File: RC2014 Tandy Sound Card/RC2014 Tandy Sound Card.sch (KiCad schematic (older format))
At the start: 15 parts, among them J1 CONN_01X39, J2 Line Out, J3 Speaker Out, J4 CONN_02X08, U1 74LS138, U2 74LS245, U3 SN76489AN, U4 TDA7056A

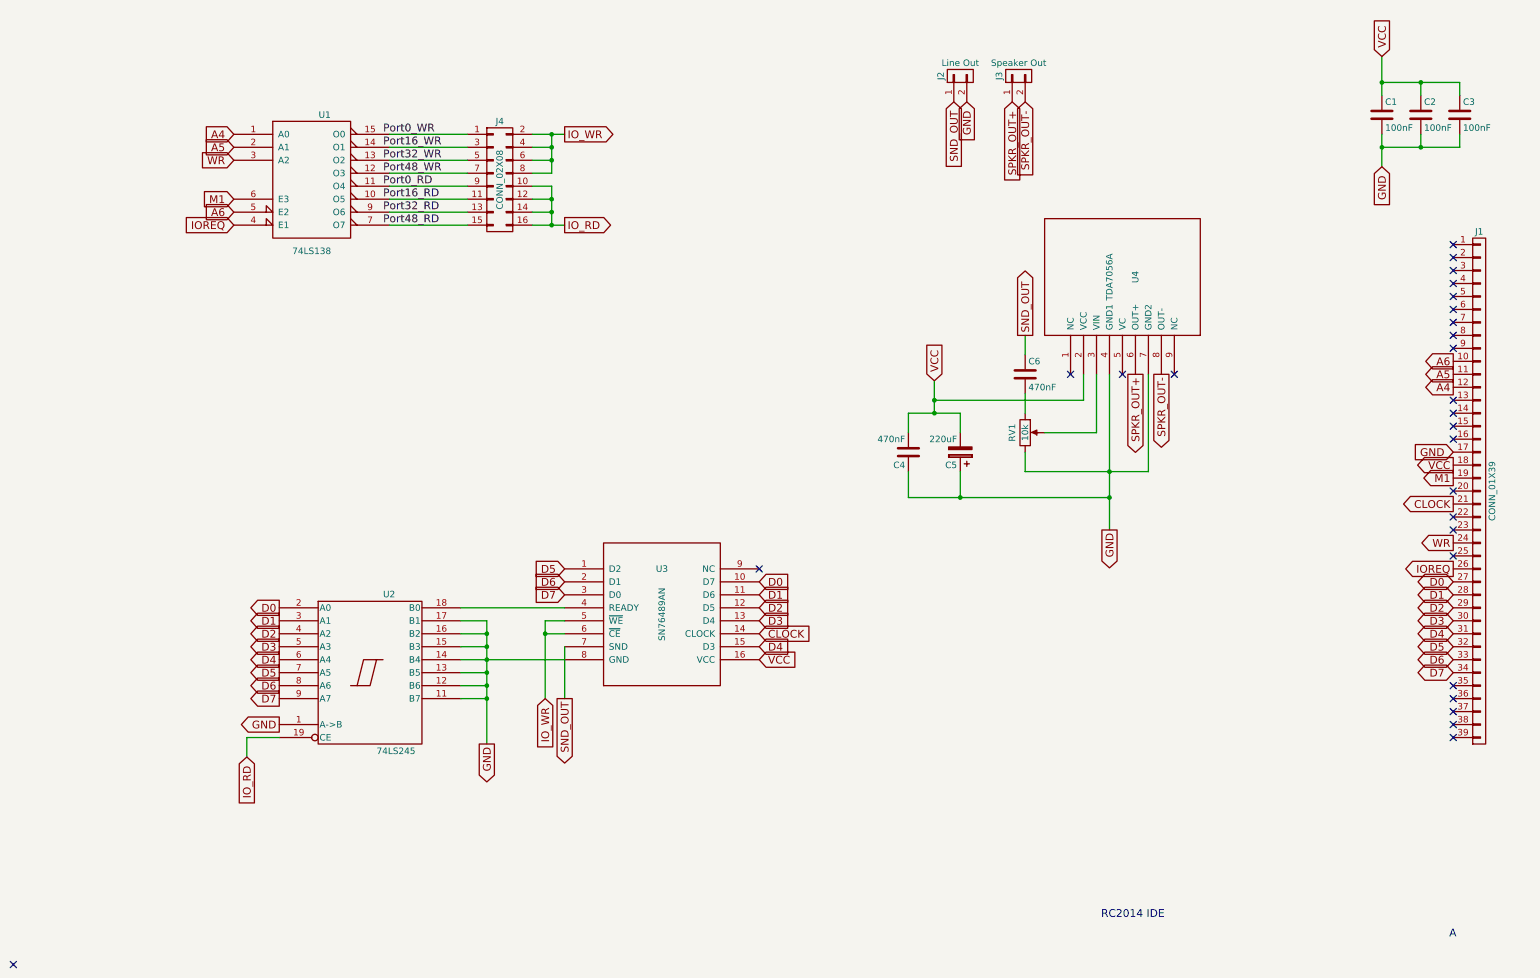
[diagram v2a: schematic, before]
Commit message: Added volume control
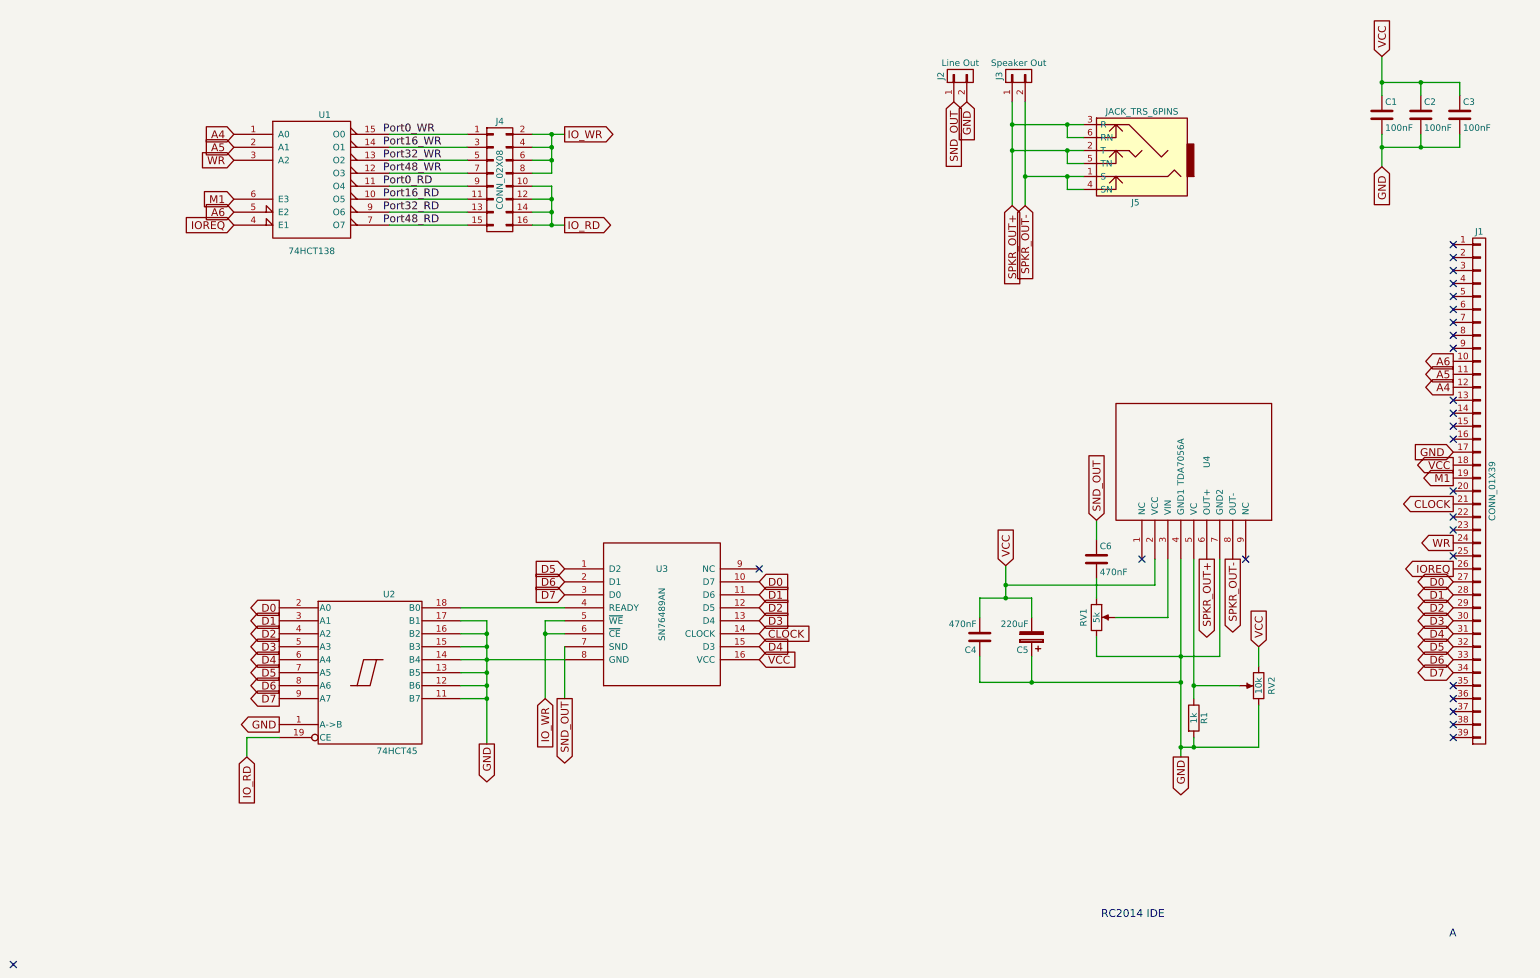
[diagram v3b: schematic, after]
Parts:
- added J5: JACK_TRS_6PINS, symbol JACK_TRS_6PINS
- added R1: 1k, symbol R
- added RV2: 10k, Potentiometers:Potentiometer_Trimmer_Bourns_3296W, symbol POT
- RV1: value 10k -> 5k
- U1: value 74LS138 -> 74HCT138
- U2: value 74LS245 -> 74HCT45
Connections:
- net GND: now also R1.2, RV2.1
- net SPKR_OUT+: now also J5.2 (T), J5.3 (R), J5.5 (TN), J5.6 (RN)
- net SPKR_OUT-: now also J5.1 (S), J5.4 (SN)
- net VCC: now also RV2.3
- net at U4.5 (VC): now also R1.1, RV2.2
- no-connect marks 27 -> 26
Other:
- moved on the sheet: C4, C5, C6, RV1, U4
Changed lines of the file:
@@
 P 1800 1800
 F 0 "U1" H 1900 2300 50  0000 C CNN
-F 1 "74LS138" H 1800 1250 50  0000 C CNN
+F 1 "74HCT138" H 1800 1250 50  0000 C CNN
 F 2 "Housings_DIP:DIP-16_W7.62mm_Socket" H 1800 1800 50  0001 C CNN
 F 3 "" H 1800 1800 50  0001 C CNN
@@
 P 2250 5600
 F 0 "U2" H 2350 6175 50  0000 L BNN
-F 1 "74LS245" H 2300 5025 50  0000 L TNN
+F 1 "74HCT45" H 2300 5025 50  0000 L TNN
 F 2 "Housings_DIP:DIP-20_W7.62mm_Socket" H 2250 5600 50  0001 C CNN
 F 3 "" H 2250 5600 50  0001 C CNN
@@
 L TDA7056A U4
 U 1 1 5917EAD4
-P 8050 2550
-F 0 "U4" H 8050 2450 50  0000 C CNN
-F 1 "TDA7056A" H 8050 2650 50  0000 C CNN
-F 2 "Pin_Headers:Pin_Header_Straight_1x09_Pitch2.54mm" H 8050 2550 50  0001 C CNN
-F 3 "DOCUMENTATION" H 8050 2550 50  0001 C CNN
-	1    8050 2550
+P 8600 3975
+F 0 "U4" H 8600 3875 50  0000 C CNN
+F 1 "TDA7056A" H 8600 4075 50  0000 C CNN
+F 2 "Pin_Headers:Pin_Header_Straight_1x09_Pitch2.54mm" H 8600 3975 50  0001 C CNN
+F 3 "DOCUMENTATION" H 8600 3975 50  0001 C CNN
+	1    8600 3975
 	0    -1   -1   0
 $EndComp
@@
 	0    -1   -1   0
 $EndComp
-Text GLabel 7950 4500 3    60   Output ~ 0
+Text GLabel 8500 6250 3    60   Output ~ 0
 GND
-Text GLabel 7200 1200 3    60   Input ~ 0
+Text GLabel 7200 2000 3    60   Input ~ 0
 SPKR_OUT+
-Text GLabel 7300 1200 3    60   Input ~ 0
+Text GLabel 7300 2000 3    60   Input ~ 0
 SPKR_OUT-
-Text GLabel 8150 3300 3    60   Output ~ 0
+Text GLabel 8700 4725 3    60   Output ~ 0
 SPKR_OUT+
-Text GLabel 8350 3300 3    60   Output ~ 0
+Text GLabel 8900 4725 3    60   Output ~ 0
 SPKR_OUT-
-Text GLabel 6600 3350 1    60   Input ~ 0
+Text GLabel 7150 4775 1    60   Input ~ 0
 VCC
-NoConn ~ 7650 3300
-NoConn ~ 8450 3300
+NoConn ~ 8200 4725
+NoConn ~ 9000 4725
 $Comp
 L C C6
 U 1 1 591812F7
-P 7300 3300
-F 0 "C6" H 7325 3400 50  0000 L CNN
-F 1 "470nF" H 7325 3200 50  0000 L CNN
-F 2 "Capacitors_THT:C_Disc_D4.7mm_W2.5mm_P5.00mm" H 7338 3150 50  0001 C CNN
-F 3 "" H 7300 3300 50  0001 C CNN
-	1    7300 3300
+P 7850 4725
+F 0 "C6" H 7875 4825 50  0000 L CNN
+F 1 "470nF" H 7875 4625 50  0000 L CNN
+F 2 "Capacitors_THT:C_Disc_D4.7mm_W2.5mm_P5.00mm" H 7888 4575 50  0001 C CNN
+F 3 "" H 7850 4725 50  0001 C CNN
+	1    7850 4725
 	1    0    0    -1
 $EndComp
@@
 L POT RV1
 U 1 1 591821C0
-P 7300 3750
-F 0 "RV1" V 7200 3750 50  0000 C CNN
-F 1 "10k" V 7300 3750 50  0000 C CNN
-F 2 "Potentiometers:Potentiometer_Trimmer_Bourns_3296W" H 7300 3750 50  0001 C CNN
-F 3 "" H 7300 3750 50  0001 C CNN
-	1    7300 3750
-	1    0    0    -1
-$EndComp
-Text GLabel 7300 3000 1    60   Output ~ 0
+P 7850 5175
+F 0 "RV1" V 7750 5175 50  0000 C CNN
+F 1 "5k" V 7850 5175 50  0000 C CNN
+F 2 "Potentiometers:Potentiometer_Trimmer_Bourns_3296W" H 7850 5175 50  0001 C CNN
+F 3 "" H 7850 5175 50  0001 C CNN
+	1    7850 5175
+	1    0    0    -1
+$EndComp
+Text GLabel 7850 4425 1    60   Input ~ 0
 SND_OUT
 $Comp
 L C C4
 U 1 1 59182F48
-P 6400 3900
-F 0 "C4" H 6425 4000 50  0000 L CNN
-F 1 "470nF" H 6425 3800 50  0000 L CNN
-F 2 "Capacitors_THT:C_Disc_D4.7mm_W2.5mm_P5.00mm" H 6438 3750 50  0001 C CNN
-F 3 "" H 6400 3900 50  0001 C CNN
-	1    6400 3900
+P 6950 5325
+F 0 "C4" H 6975 5425 50  0000 L CNN
+F 1 "470nF" H 6975 5225 50  0000 L CNN
+F 2 "Capacitors_THT:C_Disc_D4.7mm_W2.5mm_P5.00mm" H 6988 5175 50  0001 C CNN
+F 3 "" H 6950 5325 50  0001 C CNN
+	1    6950 5325
 	-1   0    0    1
 $EndComp
@@
 L CP C5
 U 1 1 59182FE8
-P 6800 3900
-F 0 "C5" H 6825 4000 50  0000 L CNN
-F 1 "220uF" H 6825 3800 50  0000 L CNN
-F 2 "Capacitors_THT:CP_Radial_D5.0mm_P2.00mm" H 6838 3750 50  0001 C CNN
-F 3 "" H 6800 3900 50  0001 C CNN
-	1    6800 3900
+P 7350 5325
+F 0 "C5" H 7375 5425 50  0000 L CNN
+F 1 "220uF" H 7375 5225 50  0000 L CNN
+F 2 "Capacitors_THT:CP_Radial_D5.0mm_P2.00mm" H 7388 5175 50  0001 C CNN
+F 3 "" H 7350 5325 50  0001 C CNN
+	1    7350 5325
 	-1   0    0    1
 $EndComp
-NoConn ~ 8050 3300
 $Comp
 L CONN_02X08 J4
@@
 Connection ~ 10350 1050
 Wire Wire Line
-	7950 3300 7950 4500
-Wire Wire Line
-	8250 4050 8250 3300
-Wire Wire Line
-	7300 4050 8250 4050
-Connection ~ 7950 4050
-Wire Wire Line
-	7450 3750 7850 3750
-Wire Wire Line
-	7850 3750 7850 3300
-Wire Wire Line
-	7300 3000 7300 3150
-Wire Wire Line
-	7300 3450 7300 3600
-Wire Wire Line
-	7300 3900 7300 4050
-Wire Wire Line
-	6600 3500 7750 3500
-Wire Wire Line
-	7750 3500 7750 3300
-Wire Wire Line
-	6400 3600 6800 3600
-Wire Wire Line
-	6800 3600 6800 3750
-Wire Wire Line
-	6400 4250 7950 4250
-Wire Wire Line
-	6800 4250 6800 4050
-Connection ~ 7950 4250
-Connection ~ 6800 4250
-Wire Wire Line
-	6400 3600 6400 3750
-Wire Wire Line
-	6400 4050 6400 4250
-Wire Wire Line
-	6600 3350 6600 3600
-Connection ~ 6600 3600
-Connection ~ 6600 3500
+	8500 4725 8500 6250
+Wire Wire Line
+	8800 5475 8800 4725
+Wire Wire Line
+	7850 5475 8800 5475
+Connection ~ 8500 5475
+Wire Wire Line
+	8000 5175 8400 5175
+Wire Wire Line
+	8400 5175 8400 4725
+Wire Wire Line
+	7850 4425 7850 4575
+Wire Wire Line
+	7850 4875 7850 5025
+Wire Wire Line
+	7850 5325 7850 5475
+Wire Wire Line
+	7150 4925 8300 4925
+Wire Wire Line
+	8300 4925 8300 4725
+Wire Wire Line
+	6950 5025 7350 5025
+Wire Wire Line
+	7350 5025 7350 5175
+Wire Wire Line
+	6950 5675 8500 5675
+Wire Wire Line
+	7350 5675 7350 5475
+Connection ~ 8500 5675
+Connection ~ 7350 5675
+Wire Wire Line
+	6950 5025 6950 5175
+Wire Wire Line
+	6950 5475 6950 5675
+Wire Wire Line
+	7150 4775 7150 5025
+Connection ~ 7150 5025
+Connection ~ 7150 4925
 Wire Wire Line
 	2400 2050 3000 2050
@@
 	3500 1550 3650 1550
 Connection ~ 3650 1550
+$Comp
+L JACK_TRS_6PINS J5
+U 1 1 593D8CEF
+P 8150 1575
+F 0 "J5" H 8150 1975 50  0000 C CNN
+F 1 "JACK_TRS_6PINS" H 8100 1275 50  0000 C CNN
+F 2 "" H 8250 1425 50  0001 C CNN
+F 3 "" H 8250 1425 50  0001 C CNN
+	1    8150 1575
+	-1   0    0    1
+$EndComp
+Wire Wire Line
+	7200 1200 7200 2000
+Wire Wire Line
+	7300 1200 7300 2000
+Wire Wire Line
+	8600 4725 8600 5800
+Wire Wire Line
+	7750 1775 7300 1775
+Connection ~ 7300 1775
+Wire Wire Line
+	7750 1875 7625 1875
+Wire Wire Line
+	7625 1875 7625 1775
+Connection ~ 7625 1775
+Wire Wire Line
+	7750 1575 7200 1575
+Connection ~ 7200 1575
+Wire Wire Line
+	7750 1375 7200 1375
+Connection ~ 7200 1375
+Wire Wire Line
+	7750 1475 7625 1475
+Wire Wire Line
+	7625 1475 7625 1375
+Connection ~ 7625 1375
+Wire Wire Line
+	7750 1675 7625 1675
+Wire Wire Line
+	7625 1675 7625 1575
+Connection ~ 7625 1575
+Text GLabel 9100 5400 1    60   Input ~ 0
+VCC
+Wire Wire Line
+	9100 6175 8500 6175
+Connection ~ 8500 6175
+$Comp
+L R R1
+U 1 1 593E8E5E
+P 8600 5950
+F 0 "R1" V 8680 5950 50  0000 C CNN
+F 1 "1k" V 8600 5950 50  0000 C CNN
+F 2 "" V 8530 5950 50  0001 C CNN
+F 3 "" H 8600 5950 50  0001 C CNN
+	1    8600 5950
+	1    0    0    -1
+$EndComp
+Wire Wire Line
+	8600 6100 8600 6175
+Connection ~ 8600 6175
+Wire Wire Line
+	9100 5400 9100 5550
+Wire Wire Line
+	9100 5850 9100 6175
+$Comp
+L POT RV2
+U 1 1 593E98E6
+P 9100 5700
+F 0 "RV2" V 9000 5700 50  0000 C CNN
+F 1 "10k" V 9100 5700 50  0000 C CNN
+F 2 "Potentiometers:Potentiometer_Trimmer_Bourns_3296W" H 9100 5700 50  0001 C CNN
+F 3 "" H 9100 5700 50  0001 C CNN
+	1    9100 5700
+	-1   0    0    1
+$EndComp
+Wire Wire Line
+	8950 5700 8600 5700
+Connection ~ 8600 5700
 $EndSCHEMATC

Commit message: Tandy Sound card revision A
PCB layout done including silkscreen. Includes TDA7056A mono amplifier circuit.
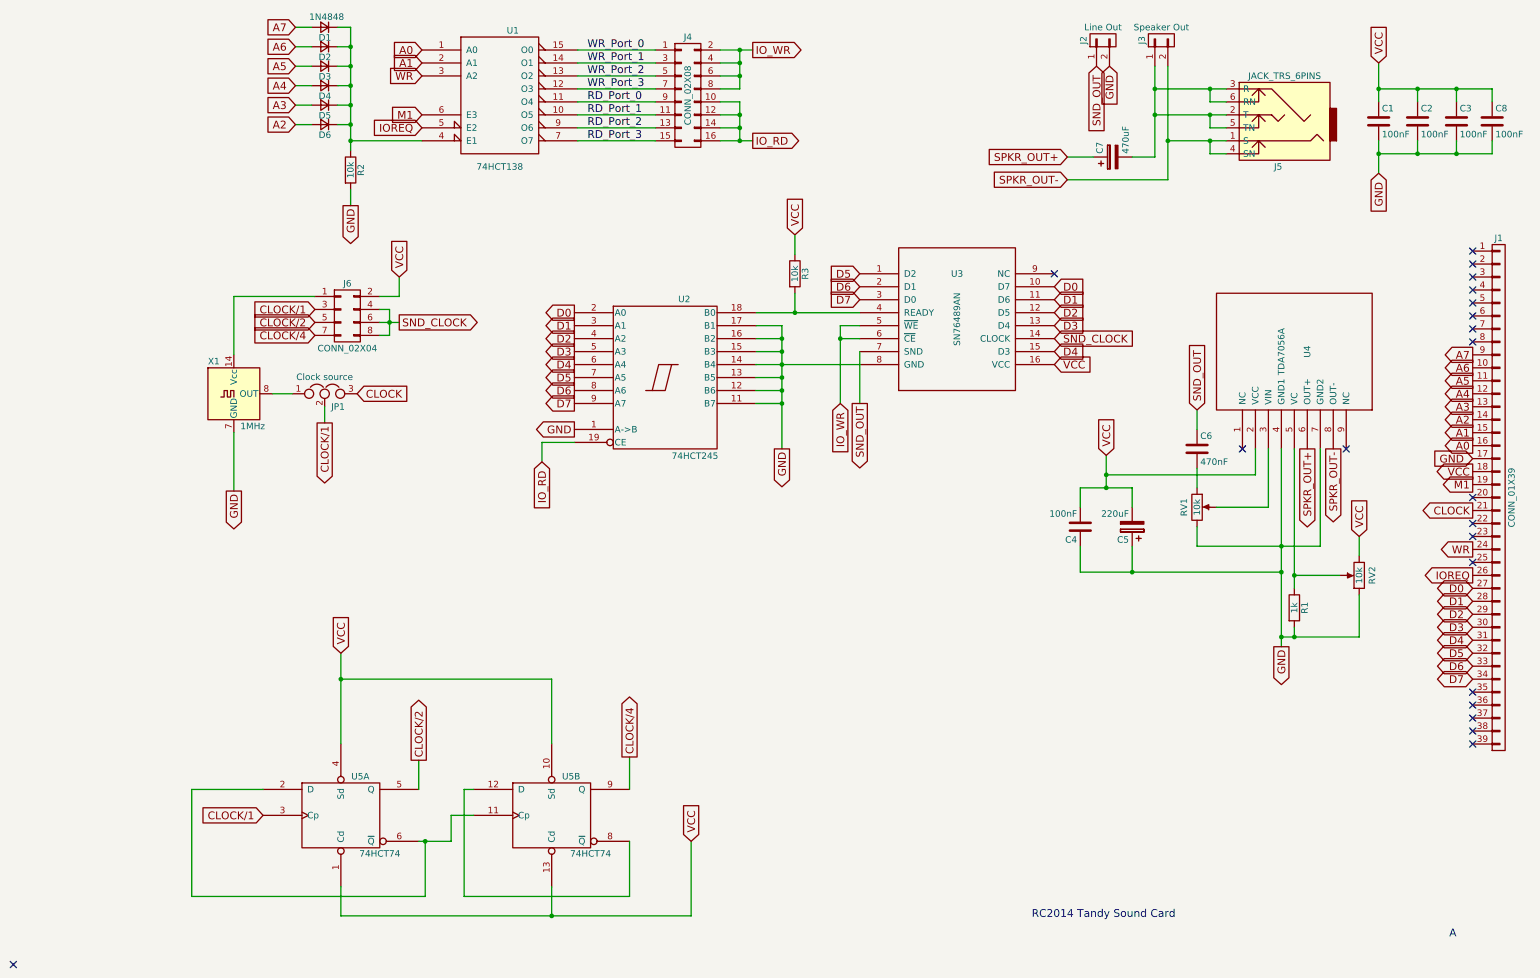
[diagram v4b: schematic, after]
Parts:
- added C7: 470uF, Capacitors_THT:CP_Radial_D5.0mm_P2.00mm, symbol CP
- added C8: 100nF, Capacitors_THT:C_Disc_D4.7mm_W2.5mm_P5.00mm, symbol C
- added D1, D2, D3, D4, D5, D6: 1N4848, Diodes_THT:D_DO-35_SOD27_P7.62mm_Horizontal, symbol D_Small
- added J6: CONN_02X04, Pin_Headers:Pin_Header_Straight_2x04_Pitch2.54mm, symbol CONN_02X04
- added JP1: Clock source, Pin_Headers:Pin_Header_Angled_1x03_Pitch2.54mm, symbol Jumper_NC_Dual
- added R2, R3: 10k, Resistors_THT:R_Axial_DIN0207_L6.3mm_D2.5mm_P10.16mm_Horizontal, symbol R
- added U5: 74HCT74, Housings_DIP:DIP-14_W7.62mm_Socket, symbol 74LS74
- added X1: 1MHz, Oscillators:Oscillator_DIP-14, symbol ACO-xxxMHz
- C4: value 470nF -> 100nF
- J5: footprint (none) -> rc2014:cliff_fcr1295_socket
- R1: footprint (none) -> Resistors_THT:R_Axial_DIN0207_L6.3mm_D2.5mm_P10.16mm_Horizontal
- RV1: value 5k -> 10k
- U2: value 74HCT45 -> 74HCT245
- U4: footprint Pin_Headers:Pin_Header_Straight_1x09_Pitch2.54mm -> Housings_SIP:SIP9_Housing
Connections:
- net A4: now also D4.2 (A); no longer U1.1 (A0)
- net A5: now also D3.2 (A); no longer U1.2 (A1)
- net A6: now also D2.2 (A); no longer U1.5 (E2)
- net CLOCK: now also JP1.3; no longer U3.14 (CLOCK)
- net GND: now also C8.2, R2.2, U5.7 (GND), U5.7 (GND), X1.7 (GND)
- net IOREQ: now also U1.5 (E2); no longer U1.4 (E1)
- net SPKR_OUT+: now also C7.1; no longer J3.1 (P1), J5.2 (T), J5.3 (R), J5.5 (TN), J5.6 (RN)
- net VCC: now also C8.1, J6.2 (P2), R3.1, U5.1 (Cd), U5.10 (Sd), U5.13 (Cd), U5.14 (VCC), U5.14 (VCC), U5.4 (Sd)
- net A3: now reaches J1.13 (P13)
- net A3: now also D5.2 (A)
- net A2: now reaches J1.14 (P14)
- net A2: now also D6.2 (A)
- net A1: now reaches J1.15 (P15)
- net A1: now also U1.2 (A1)
- net A0: now reaches J1.16 (P16)
- net A0: now also U1.1 (A0)
- net A7: now reaches J1.9 (P9)
- net A7: now also D1.2 (A)
- net RD_Port_1: now reaches J4.11 (P11), U1.10 (O5)
- net RD_Port_0: now reaches J4.9 (P9), U1.11 (O4)
- net WR_Port_3: now reaches J4.7 (P7), U1.12 (O3)
- net WR_Port_2: now reaches J4.5 (P5), U1.13 (O2)
- net WR_Port_1: now reaches J4.3 (P3), U1.14 (O1)
- net WR_Port_0: now reaches J4.1 (P1), U1.15 (O0)
- net RD_Port_3: now reaches J4.15 (P15), U1.7 (O7)
- net RD_Port_2: now reaches J4.13 (P13), U1.9 (O6)
- net at U2.18 (B0), U3.4 (READY): now also R3.2
- new net: D1.1 (K), D2.1 (K), D3.1 (K), D4.1 (K), D5.1 (K), D6.1 (K), R2.1, U1.4 (E1)
- new net: C7.2, J3.1 (P1), J5.2 (T), J5.3 (R), J5.5 (TN), J5.6 (RN)
- new net: J6.1 (P1), X1.14 (Vcc)
- new net: JP1.1, X1.8 (OUT)
- new net: U5.11 (Cp), U5.2 (D), U5.6 (~Q)
- new net: U5.12 (D), U5.8 (~Q)
- new net CLOCK/1: J6.3 (P3), JP1.2, U5.3 (Cp)
- new net CLOCK/2: J6.5 (P5), U5.5 (Q)
- new net CLOCK/4: J6.7 (P7), U5.9 (Q)
- new net SND_CLOCK: J6.4 (P4), J6.6 (P6), J6.8 (P8), U3.14 (CLOCK)
- no-connect marks 26 -> 21
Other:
- note added: "RC2014 Tandy Sound Card"
- note removed: "RC2014 IDE"
- moved on the sheet: C1, C2, C3, C4, C5, C6, J1, J2, J3, J4, J5, R1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
